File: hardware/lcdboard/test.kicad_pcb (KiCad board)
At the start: 2 copper layers, 46 x 85 mm, 29 parts, among them J1 Conn_02x16_Odd_Even_MountingP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, J2 Conn_01x45_Shielded, J3 CapTouch, U1 74CBTLV3257, U2 AP2502

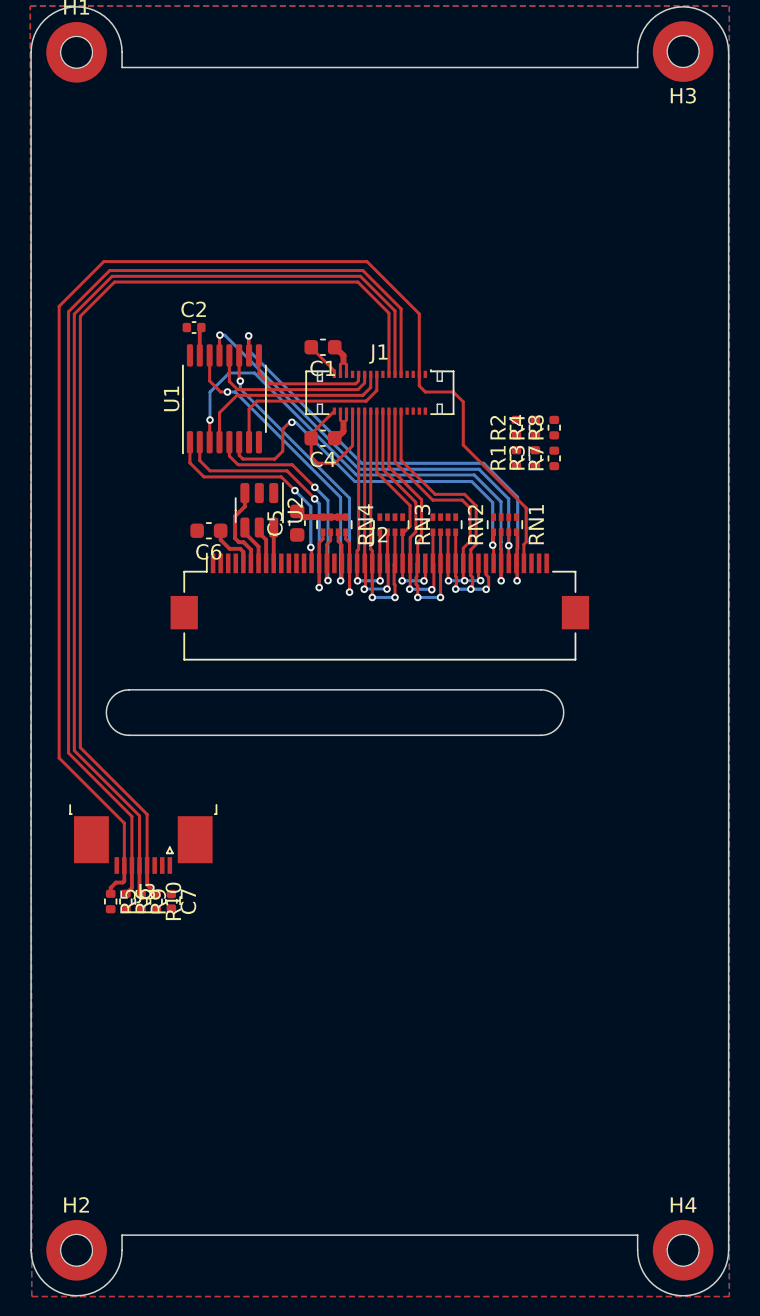
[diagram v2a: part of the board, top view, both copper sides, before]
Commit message: completed layout for lcdboard prototype, may need to move b2b down for clearance on mainboard.
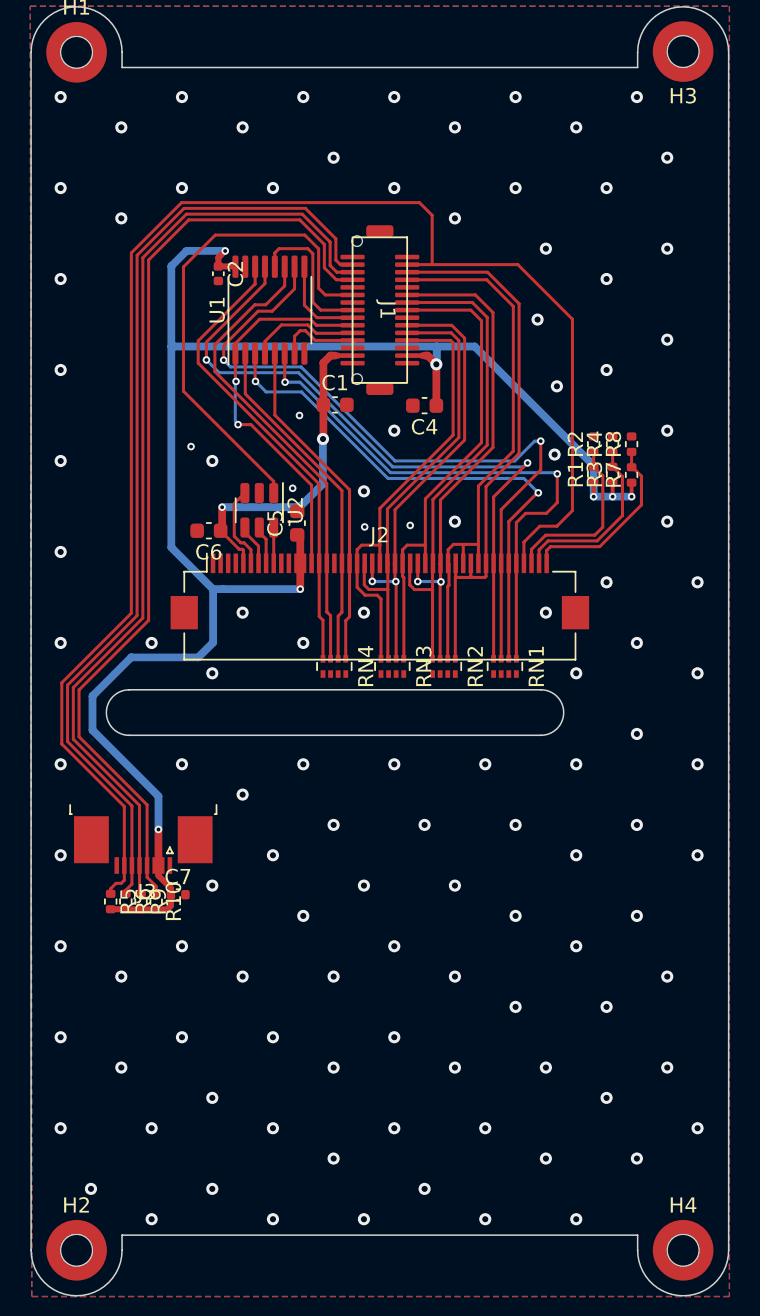
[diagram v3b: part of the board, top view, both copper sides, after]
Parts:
- J1: value Conn_02x16_Odd_Even_MountingPin -> Conn_02x15_Odd_Even_MountingPin; footprint Connector_Molex:Molex_SlimStack_502426-3210_2x16_P0.40mm_Vertical -> bt_Connector_B2B:10132798-031100LF
- moved RN3 9.35 mm to (146.1, 117.2)
- moved RN2 9.35 mm to (149.5, 117.2)
- moved RN1 9.35 mm to (153.5, 117.2)
- moved RN4 9.35 mm to (142.2, 117.2)
- moved C4 7.04 mm to (148.2, 100.0)
- moved U1 6.57 mm to (138.0, 93.8)
- moved J1 5.45 mm to (145.2, 93.8), turned to -90 degrees
- moved R1 5.22 mm to (159.3, 104.6)
- moved R2 5.22 mm to (159.3, 102.6)
- moved R3 5.22 mm to (160.6, 104.6)
- moved R4 5.22 mm to (160.6, 102.6)
- moved R7 5.22 mm to (161.8, 104.6)
- moved R8 5.22 mm to (161.8, 102.6)
- moved C2 3.89 mm to (134.6, 91.3), turned to -90 degrees
- moved C1 3.88 mm to (142.3, 100.0), turned to 0 degrees
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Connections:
- C1 pad 1: VDD_AUX_3V3 -> VDD_NVDC
- C4 pad 1: VDD_NVDC -> VDD_AUX_3V3
- J1 pad 10: /LCD_RGB.B1 -> /LCD_RGB.R2
- J1 pad 11: /TOUCH_SDA -> /LCD_RGB.R1
- J1 pad 12: /LCD_RGB.B0 -> /LCD_RGB.R0
- J1 pad 13: /TOUCH_SCL -> GND
- J1 pad 14: /LCD_RGB.G2 -> VDD_AUX_3V3
- J1 pad 15: /LCD_SPI_CS -> GND
- J1 pad 16: /LCD_RGB.G1 -> GND
- J1 pad 17: /LCD_MUX0 -> VDD_NVDC
- J1 pad 18: /LCD_RGB.G0 -> GND
- J1 pad 19: /LCD_MUX1 -> /LCD_MUX3
- J1 pad 2: GND -> ~{RESET}
- J1 pad 20: /LCD_RGB.R2 -> /LCD_MUX2
- J1 pad 21: /LCD_MUX2 -> /LCD_SPI_CS
- J1 pad 22: /LCD_RGB.R1 -> /LCD_MUX1
- J1 pad 23: /LCD_MUX3 -> /LCD_MUX0
- J1 pad 24: /LCD_RGB.R0 -> GND
- J1 pad 25: GND -> /DISPLAY_BL
- J1 pad 27: VDD_AUX_3V3 -> /TOUCH_SCL
- J1 pad 28: VDD_NVDC -> /TOUCH_SDA
- J1 pad 29: VDD_AUX_3V3 -> /TOUCH_INT
- J1 pad 3: ~{RESET} -> /LCD_RGB.B1
- J1 pad 30: VDD_NVDC -> GND
- J1 pad 4: unconnected-(J1-Pad4) -> /LCD_RGB.B0
- J1 pad 5: /DISPLAY_BL -> GND
- J1 pad 6: unconnected-(J1-Pad6) -> /LCD_RGB.G2
- J1 pad 7: GND -> /LCD_RGB.G1
- J1 pad 8: GND -> /LCD_RGB.G0
- J1 pad 9: /TOUCH_INT -> GND
- RN1 pad 1: GND -> /LCD_CTRL.VSYNC
- RN1 pad 2: GND -> /LCD_CTRL.HSYNC
- RN1 pad 3: GND -> /LCD_CTRL.PCLK
- RN1 pad 4: GND -> /LCD_CTRL.DE
- RN1 pad 5: /LCD_CTRL.DE -> GND
- RN1 pad 6: /LCD_CTRL.PCLK -> GND
- RN1 pad 7: /LCD_CTRL.HSYNC -> GND
- RN1 pad 8: /LCD_CTRL.VSYNC -> GND
- RN2 pad 1: GND -> /LCD_RGB.B1
- RN2 pad 2: GND -> /LCD_RGB.B0
- RN2 pad 3: GND -> /LCD_RGB.G2
- RN2 pad 4: GND -> /LCD_RGB.G1
- RN2 pad 5: /LCD_RGB.G1 -> GND
- RN2 pad 6: /LCD_RGB.G2 -> GND
- RN2 pad 7: /LCD_RGB.B0 -> GND
- RN2 pad 8: /LCD_RGB.B1 -> GND
- RN3 pad 1: GND -> /LCD_RGB.G0
- RN3 pad 2: GND -> /LCD_RGB.R2
- RN3 pad 3: GND -> /LCD_RGB.R1
- RN3 pad 4: GND -> /LCD_RGB.R0
- RN3 pad 5: /LCD_RGB.R0 -> GND
- RN3 pad 6: /LCD_RGB.R1 -> GND
- RN3 pad 7: /LCD_RGB.R2 -> GND
- RN3 pad 8: /LCD_RGB.G0 -> GND
- RN4 pad 1: GND -> /LCD_SPI.MISO
- RN4 pad 2: GND -> /LCD_SPI.MOSI
- RN4 pad 3: GND -> /LCD_SPI.SCLK
- RN4 pad 4: GND -> /LCD_SPI.DC
- RN4 pad 5: /LCD_SPI.DC -> GND
- RN4 pad 6: /LCD_SPI.SCLK -> GND
- RN4 pad 7: /LCD_SPI.MOSI -> GND
- RN4 pad 8: /LCD_SPI.MISO -> GND
- U1 pad 10: /LCD_CTRL.VSYNC -> /LCD_CTRL.PCLK
- U1 pad 11: /LCD_SPI.MISO -> /LCD_SPI.SCLK
- U1 pad 12: /LCD_MUX2 -> /LCD_MUX0
- U1 pad 13: /LCD_CTRL.HSYNC -> /LCD_CTRL.DE
- U1 pad 14: /LCD_SPI.MOSI -> /LCD_SPI.DC
- U1 pad 2: /LCD_SPI.DC -> /LCD_SPI.MOSI
- U1 pad 3: /LCD_CTRL.PCLK -> /LCD_CTRL.HSYNC
- U1 pad 4: /LCD_MUX1 -> /LCD_MUX2
- U1 pad 5: /LCD_SPI.SCLK -> /LCD_SPI.MISO
- U1 pad 6: /LCD_CTRL.DE -> /LCD_CTRL.VSYNC
- U1 pad 7: /LCD_MUX0 -> /LCD_MUX3
- U1 pad 9: /LCD_MUX3 -> /LCD_MUX1
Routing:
- net VDD_AUX_3V3: track 3.13 -> 116.8 mm, vias 0 -> 7
- net /DISPLAY_BL: track 0.00 -> 32.6 mm
- net /LCD_CTRL.DE: track 26.6 -> 45.8 mm
- net GND: track 17.1 -> 0.00 mm, vias 0 -> 117
- net /LCD_RGB.G0: track 15.1 -> 31.6 mm, vias 2 -> 0
- net VDD_NVDC: track 6.23 -> 22.7 mm, vias 0 -> 2
- net /LCD_RGB.B0: track 21.1 -> 36.5 mm, vias 3 -> 0
- net /LCD_RGB.G1: track 18.1 -> 33.2 mm, vias 2 -> 0
- net /LCD_SPI.SCLK: track 17.2 -> 31.4 mm, vias 2 -> 0
- net /LCD_RGB.G2: track 19.2 -> 33.3 mm
- net /LCD_RGB.B1: track 22.8 -> 36.9 mm, vias 3 -> 0
- net ~{RESET}: track 88.1 -> 101.7 mm
- net /LCD_RGB.R0: track 16.0 -> 29.6 mm, vias 2 -> 0
- net /LCD_CTRL.PCLK: track 35.0 -> 48.3 mm
- net /LCD_RGB.R1: track 17.1 -> 29.8 mm, vias 2 -> 0
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
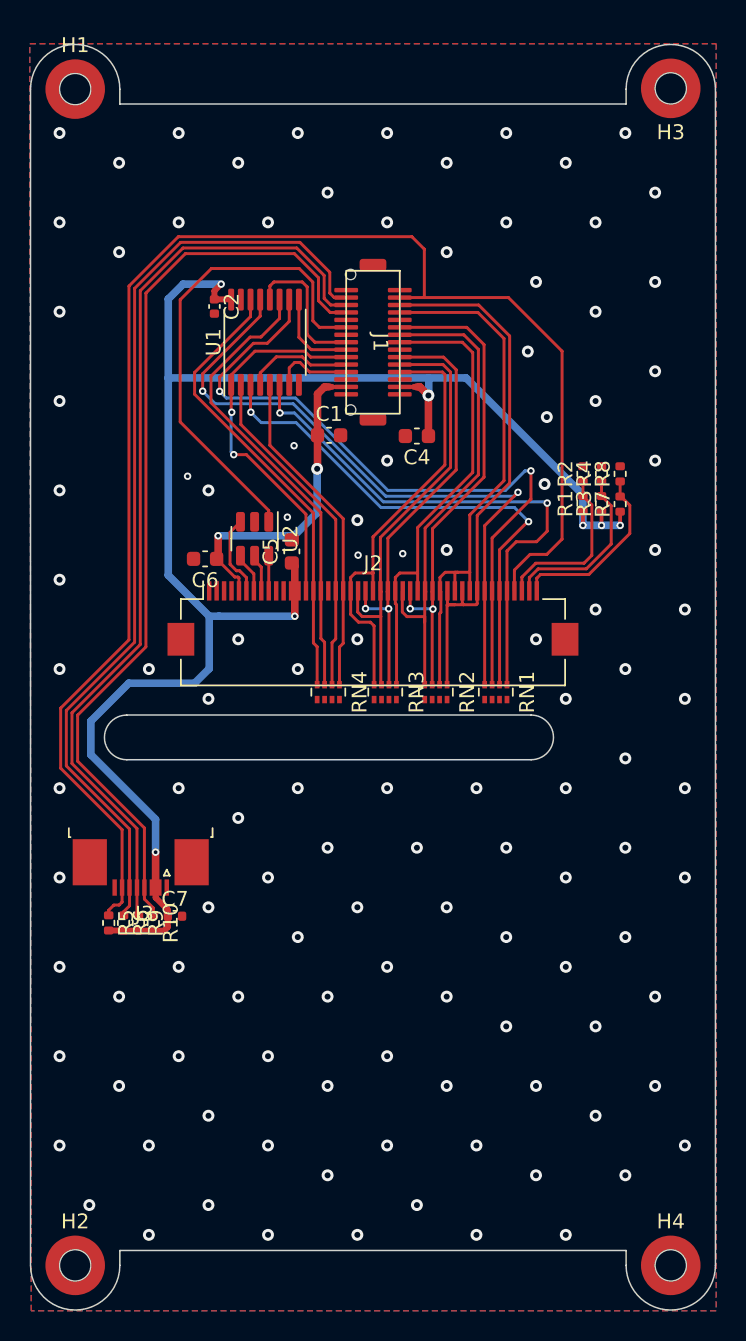
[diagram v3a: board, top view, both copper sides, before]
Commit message: relayout screen
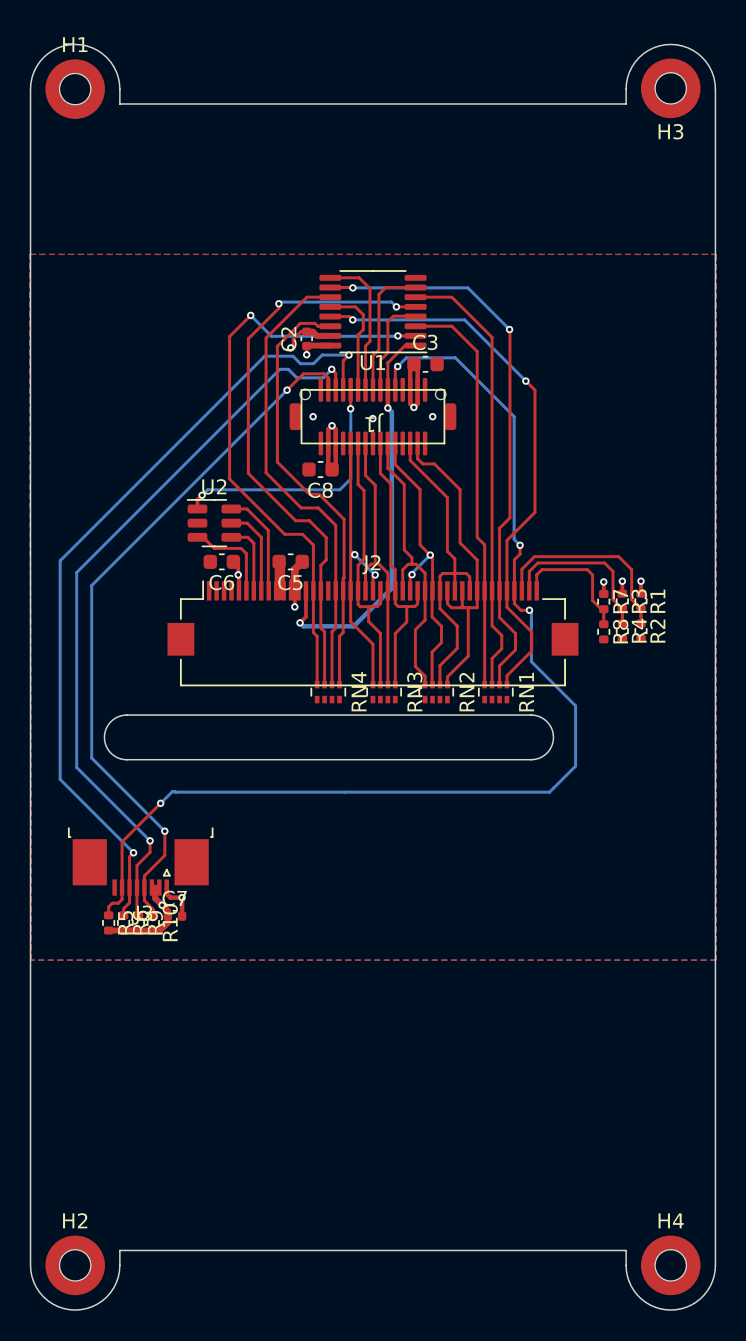
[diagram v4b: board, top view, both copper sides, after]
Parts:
- removed C1, C4: 1u, Capacitor_SMD:C_0603_1608Metric
- added C3: 1u, Capacitor_SMD:C_0603_1608Metric, F.Cu at (148.8, 95.2)
- added C8: 1u, Capacitor_SMD:C_0603_1608Metric, F.Cu at (141.7, 102.3)
- moved R2 11.3 mm to (163.2, 113.2), turned to -90 degrees
- moved R8 10.7 mm to (160.8, 113.2), turned to -90 degrees
- moved R4 10.7 mm to (162.0, 113.2), turned to -90 degrees
- moved R1 7.63 mm to (163.2, 111.2), turned to -90 degrees
- moved U1 7.53 mm to (145.2, 91.7), turned to 180 degrees
- moved R3 6.71 mm to (162.0, 111.2), turned to -90 degrees
- moved R7 6.64 mm to (160.8, 111.2), turned to -90 degrees
- moved C2 6.57 mm to (140.8, 93.5), turned to 90 degrees
- moved J1 5.00 mm to (145.2, 98.8), turned to 180 degrees
- moved U2 2.90 mm to (134.6, 105.9), turned to 0 degrees
- moved C6 1.14 mm to (135.1, 108.5)
- moved C5 0.70 mm to (139.7, 108.5), turned to 180 degrees
- moved RN3 0.07 mm to (146.0, 117.2)
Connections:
- C6 pad 1: VDD_NVDC -> VDD_AUX_3V3
- H1 pad 1: GND -> unconnected-(H1-Pad1)
- H2 pad 1: GND -> unconnected-(H2-Pad1)
- H3 pad 1: GND -> unconnected-(H3-Pad1)
- H4 pad 1: GND -> unconnected-(H4-Pad1)
- J1 pad 10: /LCD_RGB.R2 -> /LCD_RGB.R1
- J1 pad 11: /LCD_RGB.R1 -> /LCD_RGB.R0
- J1 pad 12: /LCD_RGB.R0 -> GND
- J1 pad 13: GND -> VDD_AUX_3V3
- J1 pad 17: VDD_NVDC -> /TOUCH_SCL
- J1 pad 18: GND -> /TOUCH_SDA
- J1 pad 19: /LCD_MUX3 -> /TOUCH_INT
- J1 pad 2: ~{RESET} -> /LCD_RGB.B1
- J1 pad 20: /LCD_MUX2 -> /DISPLAY_BL
- J1 pad 21: /LCD_SPI_CS -> /LCD_MUX0
- J1 pad 23: /LCD_MUX0 -> /LCD_MUX2
- J1 pad 24: GND -> /LCD_MUX3
- J1 pad 25: /DISPLAY_BL -> /LCD_SPI_CS
- J1 pad 26: GND -> ~{RESET}
- J1 pad 27: /TOUCH_SCL -> GND
- J1 pad 28: /TOUCH_SDA -> VDD_AUX_3V3
- J1 pad 29: /TOUCH_INT -> VDD_AUX_3V3
- J1 pad 3: /LCD_RGB.B1 -> /LCD_RGB.B0
- J1 pad 4: /LCD_RGB.B0 -> GND
- J1 pad 5: GND -> /LCD_RGB.G2
- J1 pad 6: /LCD_RGB.G2 -> /LCD_RGB.G1
- J1 pad 7: /LCD_RGB.G1 -> /LCD_RGB.G0
- J1 pad 8: /LCD_RGB.G0 -> GND
- J1 pad 9: GND -> /LCD_RGB.R2
- J2 pad 5: VDD_NVDC -> VDD_AUX_3V3
- U1 pad 10: /LCD_CTRL.PCLK -> /LCD_CTRL.HSYNC
- U1 pad 11: /LCD_SPI.SCLK -> /LCD_SPI.MOSI
- U1 pad 13: /LCD_CTRL.DE -> /LCD_CTRL.VSYNC
- U1 pad 14: /LCD_SPI.DC -> /LCD_SPI.MISO
- U1 pad 2: /LCD_SPI.MOSI -> /LCD_SPI.DC
- U1 pad 3: /LCD_CTRL.HSYNC -> /LCD_CTRL.DE
- U1 pad 4: /LCD_MUX2 -> /LCD_MUX3
- U1 pad 5: /LCD_SPI.MISO -> /LCD_SPI.SCLK
- U1 pad 6: /LCD_CTRL.VSYNC -> /LCD_CTRL.PCLK
- U1 pad 7: /LCD_MUX3 -> /LCD_MUX2
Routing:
- net VDD_AUX_3V3: track 116.8 -> 32.8 mm, vias 7 -> 9
- net ~{RESET}: track 101.7 -> 75.5 mm, vias 0 -> 4
- net VDD_NVDC: track 22.7 -> 0.00 mm, vias 2 -> 0
- net /LCD_CTRL.DE: track 45.8 -> 27.4 mm, vias 2 -> 0
- net /LCD_CTRL.PCLK: track 48.3 -> 30.1 mm, vias 2 -> 0
- net /TOUCH_SCL: track 62.9 -> 47.7 mm, vias 0 -> 2
- net /DISPLAY_BL: track 32.6 -> 17.5 mm, vias 0 -> 2
- net /LCD_RGB.B0: track 36.5 -> 22.6 mm
- net /LCD_RGB.B1: track 36.9 -> 23.1 mm
- net /LCD_RGB.G1: track 33.2 -> 20.1 mm
- net /TOUCH_SDA: track 63.2 -> 50.2 mm, vias 0 -> 2
- net GND: track 0.00 -> 12.7 mm, vias 117 -> 5
- net /LCD_RGB.G2: track 33.3 -> 20.7 mm
- net /LCD_RGB.G0: track 31.6 -> 19.3 mm
- net /LCD_RGB.R2: track 30.1 -> 19.2 mm, vias 2 -> 0
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- added copper zone on In1.Cu, net GND
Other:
- copper layers 2 -> 4

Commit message: testing viastiching
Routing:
- net GND: track 12.7 -> 34.0 mm, vias 5 -> 11
- net ~{RESET}: track 75.5 -> 76.9 mm, vias 4 -> 3
- net /TOUCH_INT: track 54.2 -> 53.1 mm
- net /LCD_SPI.DC: track 40.2 -> 39.3 mm
- net /TOUCH_SDA: track 50.2 -> 49.4 mm
- net /LCD_RGB.R0: track 20.3 -> 20.9 mm

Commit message: screen design freeze, 3d model added to base, routed display connector, sd, usb
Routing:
- net GND: vias 11 -> 110
- added copper zone on In2.Cu, net VDD_AUX_3V3
